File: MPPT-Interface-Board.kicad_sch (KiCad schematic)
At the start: 29 parts, among them J1 MPPT A, J2 MPPT X, J3 CarCAN In, J4 CarCAN Out, J5 FUSEBOX, Q1 PMV35EPER, U1 RI3-1209S

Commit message: uhm so why am i so stupid
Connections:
- net +12V: no longer C4.1
- net +12V_PROT: now also C4.1
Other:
- moved on the sheet: C3, C4
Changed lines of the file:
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@@
 	(wire
 		(pts
-			(xy 204.47 100.33) (xy 207.01 100.33)
+			(xy 204.47 100.33) (xy 208.28 100.33)
 		)
 		(stroke
@@
 	(wire
 		(pts
-			(xy 207.01 88.9) (xy 204.47 88.9)
+			(xy 208.28 88.9) (xy 204.47 88.9)
 		)
 		(stroke
@@
 	(wire
 		(pts
-			(xy 214.63 100.33) (xy 217.17 100.33)
+			(xy 215.9 100.33) (xy 219.71 100.33)
 		)
 		(stroke
@@
 	(wire
 		(pts
-			(xy 214.63 88.9) (xy 217.17 88.9)
+			(xy 215.9 88.9) (xy 219.71 88.9)
 		)
 		(stroke
@@
 	(wire
 		(pts
-			(xy 217.17 88.9) (xy 217.17 86.36)
+			(xy 219.71 88.9) (xy 219.71 86.36)
 		)
 		(stroke
@@
 	(wire
 		(pts
-			(xy 217.17 100.33) (xy 217.17 102.87)
+			(xy 219.71 100.33) (xy 219.71 102.87)
 		)
 		(stroke
@@
 	(rectangle
 		(start 198.12 78.74)
-		(end 223.52 114.3)
+		(end 226.06 114.3)
 		(stroke
 			(width 0)
@@
 		(exclude_from_sim no)
 		(at 198.12 110.49 0)
-		(size 25.4 3.81)
+		(size 27.94 3.81)
 		(stroke
 			(width 0)
@@
 	)
 	(symbol
+		(lib_id "power:+12V")
+		(at 204.47 86.36 0)
+		(unit 1)
+		(exclude_from_sim no)
+		(in_bom yes)
+		(on_board yes)
+		(dnp no)
+		(property "Reference" "#PWR021"
+			(at 204.47 90.17 0)
+			(effects
+				(font
+					(size 1.27 1.27)
+				)
+				(hide yes)
+			)
+		)
+		(property "Value" "+12V_PROT"
+			(at 198.882 82.55 0)
+			(effects
+				(font
+					(size 1.27 1.27)
+				)
+				(justify left)
+			)
+		)
+		(property "Footprint" ""
+			(at 204.47 86.36 0)
+			(effects
+				(font
+					(size 1.27 1.27)
+				)
+				(hide yes)
+			)
+		)
+		(property "Datasheet" ""
+			(at 204.47 86.36 0)
+			(effects
+				(font
+					(size 1.27 1.27)
+				)
+				(hide yes)
+			)
+		)
+		(property "Description" "Power symbol creates a global label with name \"+12V\""
+			(at 204.47 86.36 0)
+			(effects
+				(font
+					(size 1.27 1.27)
+				)
+				(hide yes)
+			)
+		)
+		(pin "1"
+		)
+		(instances
+			(project "MPPT-Interface-Board"
+				(path "/b7de5949-1fc3-44b6-95a7-0faccc8a2b33"
+					(reference "#PWR021")
+					(unit 1)
+				)
+			)
+		)
+	)
+	(symbol
 		(lib_id "power:GND")
 		(at 63.5 97.79 0)
@@
 	)
 	(symbol
-		(lib_id "power:+12V")
-		(at 204.47 86.36 0)
-		(unit 1)
-		(exclude_from_sim no)
-		(in_bom yes)
-		(on_board yes)
-		(dnp no)
-		(property "Reference" "#PWR021"
-			(at 204.47 90.17 0)
-			(effects
-				(font
-					(size 1.27 1.27)
-				)
-				(hide yes)
-			)
-		)
-		(property "Value" "+12V"
-			(at 201.676 82.55 0)
-			(effects
-				(font
-					(size 1.27 1.27)
-				)
-				(justify left)
-			)
-		)
-		(property "Footprint" ""
-			(at 204.47 86.36 0)
-			(effects
-				(font
-					(size 1.27 1.27)
-				)
-				(hide yes)
-			)
-		)
-		(property "Datasheet" ""
-			(at 204.47 86.36 0)
-			(effects
-				(font
-					(size 1.27 1.27)
-				)
-				(hide yes)
-			)
-		)
-		(property "Description" "Power symbol creates a global label with name \"+12V\""
-			(at 204.47 86.36 0)
-			(effects
-				(font
-					(size 1.27 1.27)
-				)
-				(hide yes)
-			)
-		)
-		(pin "1"
-		)
-		(instances
-			(project "MPPT-Interface-Board"
-				(path "/b7de5949-1fc3-44b6-95a7-0faccc8a2b33"
-					(reference "#PWR021")
-					(unit 1)
-				)
-			)
-		)
-	)
-	(symbol
 		(lib_id "Device:R")
 		(at 139.7 92.71 0)
@@
 	(symbol
 		(lib_id "power:GND")
-		(at 217.17 102.87 0)
+		(at 219.71 102.87 0)
 		(unit 1)
 		(exclude_from_sim no)
@@
 		(dnp no)
 		(property "Reference" "#PWR020"
-			(at 217.17 109.22 0)
+			(at 219.71 109.22 0)
 			(effects
 				(font
@@
 		)
 		(property "Value" "CGND"
-			(at 217.17 106.934 0)
+			(at 219.71 106.934 0)
 			(effects
 				(font
@@
 		)
 		(property "Footprint" ""
-			(at 217.17 102.87 0)
+			(at 219.71 102.87 0)
 			(effects
 				(font
@@
 		)
 		(property "Datasheet" ""
-			(at 217.17 102.87 0)
+			(at 219.71 102.87 0)
 			(effects
 				(font
@@
 		)
 		(property "Description" "Power symbol creates a global label with name \"GND\" , ground"
-			(at 217.17 102.87 0)
+			(at 219.71 102.87 0)
 			(effects
 				(font
@@
 	(symbol
 		(lib_id "Device:C")
-		(at 210.82 88.9 90)
+		(at 212.09 88.9 90)
 		(unit 1)
 		(exclude_from_sim no)
@@
 		(dnp no)
 		(property "Reference" "C4"
-			(at 210.82 82.804 90)
+			(at 212.09 82.804 90)
 			(effects
 				(font
@@
 		)
 		(property "Value" "470p"
-			(at 210.82 85.09 90)
+			(at 212.09 85.09 90)
 			(effects
 				(font
@@
 		)
 		(property "Footprint" "Capacitor_SMD:C_0805_2012Metric"
-			(at 214.63 87.9348 0)
+			(at 215.9 87.9348 0)
 			(effects
 				(font
@@
 		)
 		(property "Datasheet" "~"
-			(at 210.82 88.9 0)
+			(at 212.09 88.9 0)
 			(effects
 				(font
@@
 		)
 		(property "Description" "Unpolarized capacitor"
-			(at 210.82 88.9 0)
+			(at 212.09 88.9 0)
 			(effects
 				(font
@@
 		)
 		(property "P/N" "08053C471JAT2A"
-			(at 210.82 88.9 0)
+			(at 212.09 88.9 0)
 			(effects
 				(font
@@
 	(symbol
 		(lib_id "power:+12V")
-		(at 217.17 86.36 0)
+		(at 219.71 86.36 0)
 		(unit 1)
 		(exclude_from_sim no)
@@
 		(dnp no)
 		(property "Reference" "#PWR022"
-			(at 217.17 90.17 0)
+			(at 219.71 90.17 0)
 			(effects
 				(font
@@
 		)
 		(property "Value" "V_CAN"
-			(at 214.122 82.55 0)
+			(at 216.662 82.55 0)
 			(effects
 				(font
@@
 		)
 		(property "Footprint" ""
-			(at 217.17 86.36 0)
+			(at 219.71 86.36 0)
 			(effects
 				(font
@@
 		)
 		(property "Datasheet" ""
-			(at 217.17 86.36 0)
+			(at 219.71 86.36 0)
 			(effects
 				(font
@@
 		)
 		(property "Description" "Power symbol creates a global label with name \"+12V\""
-			(at 217.17 86.36 0)
+			(at 219.71 86.36 0)
 			(effects
 				(font
@@
 	(symbol
 		(lib_id "Device:C")
-		(at 210.82 100.33 90)
+		(at 212.09 100.33 90)
 		(unit 1)
 		(exclude_from_sim no)
@@
 		(dnp no)
 		(property "Reference" "C3"
-			(at 210.82 94.234 90)
+			(at 212.09 94.234 90)
 			(effects
 				(font
@@
 		)
 		(property "Value" "330p"
-			(at 210.82 96.266 90)
+			(at 212.09 96.266 90)
 			(effects
 				(font
@@
 		)
 		(property "Footprint" "Capacitor_SMD:C_0805_2012Metric"
-			(at 214.63 99.3648 0)
+			(at 215.9 99.3648 0)
 			(effects
 				(font
@@
 		)
 		(property "Datasheet" "~"
-			(at 210.82 100.33 0)
+			(at 212.09 100.33 0)
 			(effects
 				(font
@@
 		)
 		(property "Description" "Unpolarized capacitor"
-			(at 210.82 100.33 0)
+			(at 212.09 100.33 0)
 			(effects
 				(font
@@
 		)
 		(property "P/N" "08053A331JAT2A"
-			(at 210.82 100.33 0)
+			(at 212.09 100.33 0)
 			(effects
 				(font

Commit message: initial layout (unrouted)
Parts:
- added H1, H2, H3, H4: MountingHole, MountingHole:MountingHole_3mm, symbol Mechanical:MountingHole
- TP6: value CGND -> CGND2
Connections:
- net CAN_H: no longer R1.2
- net CAN_H2: now also R1.2
- net CAN_L: no longer JP1.2 (B)
- net CAN_L2: now also JP1.2 (B)
- net CGND: no longer TP6.1
- net CGND2: now also TP6.1

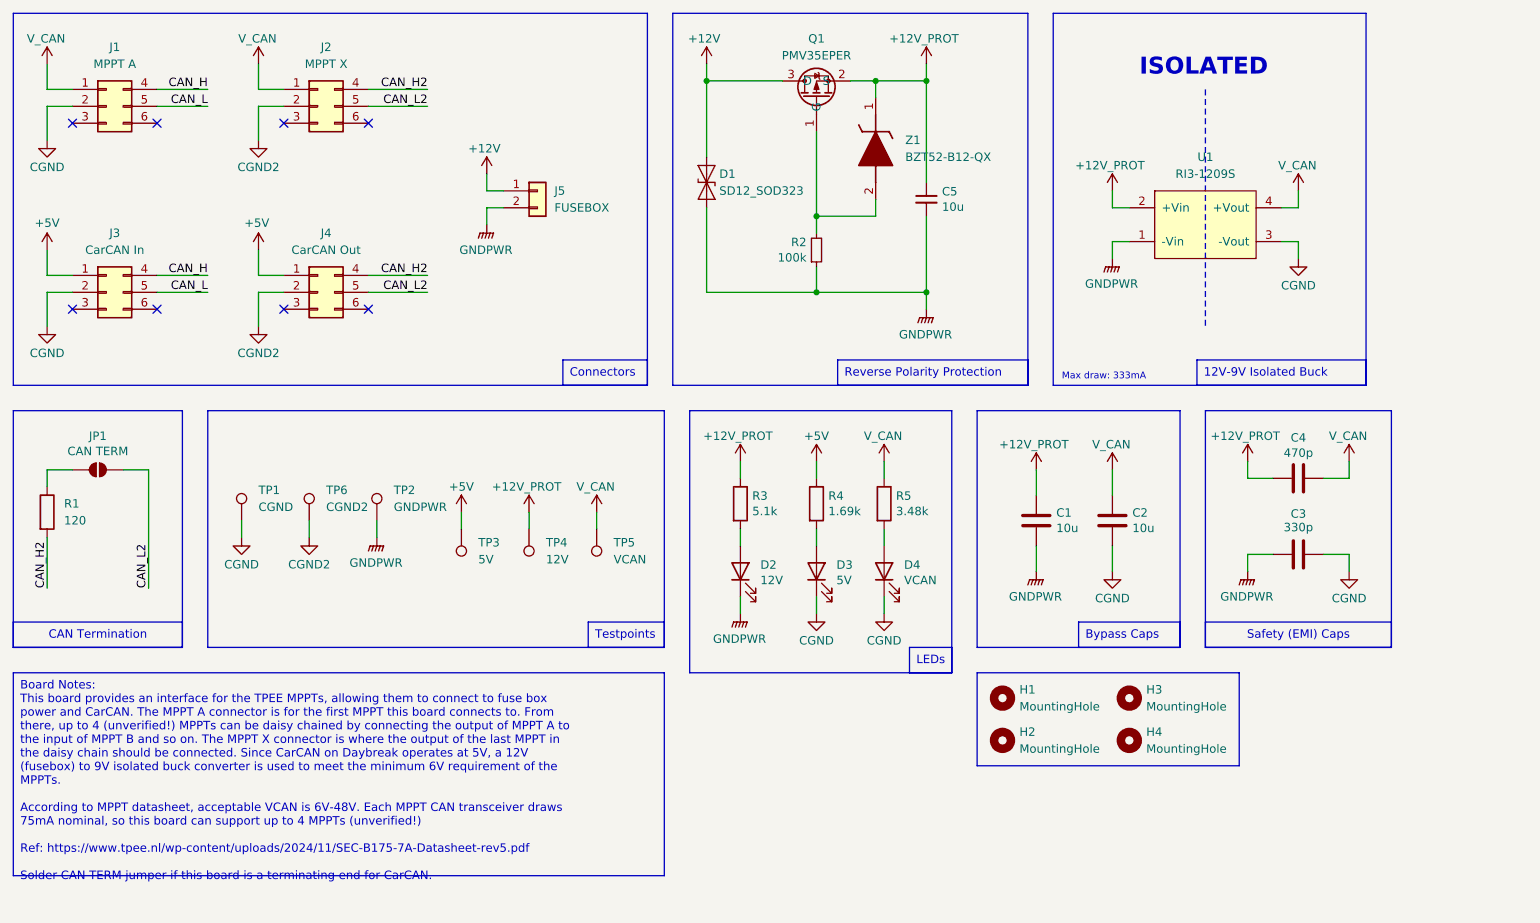
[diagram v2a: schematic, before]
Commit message: change carcan to 4 pin & add start termination
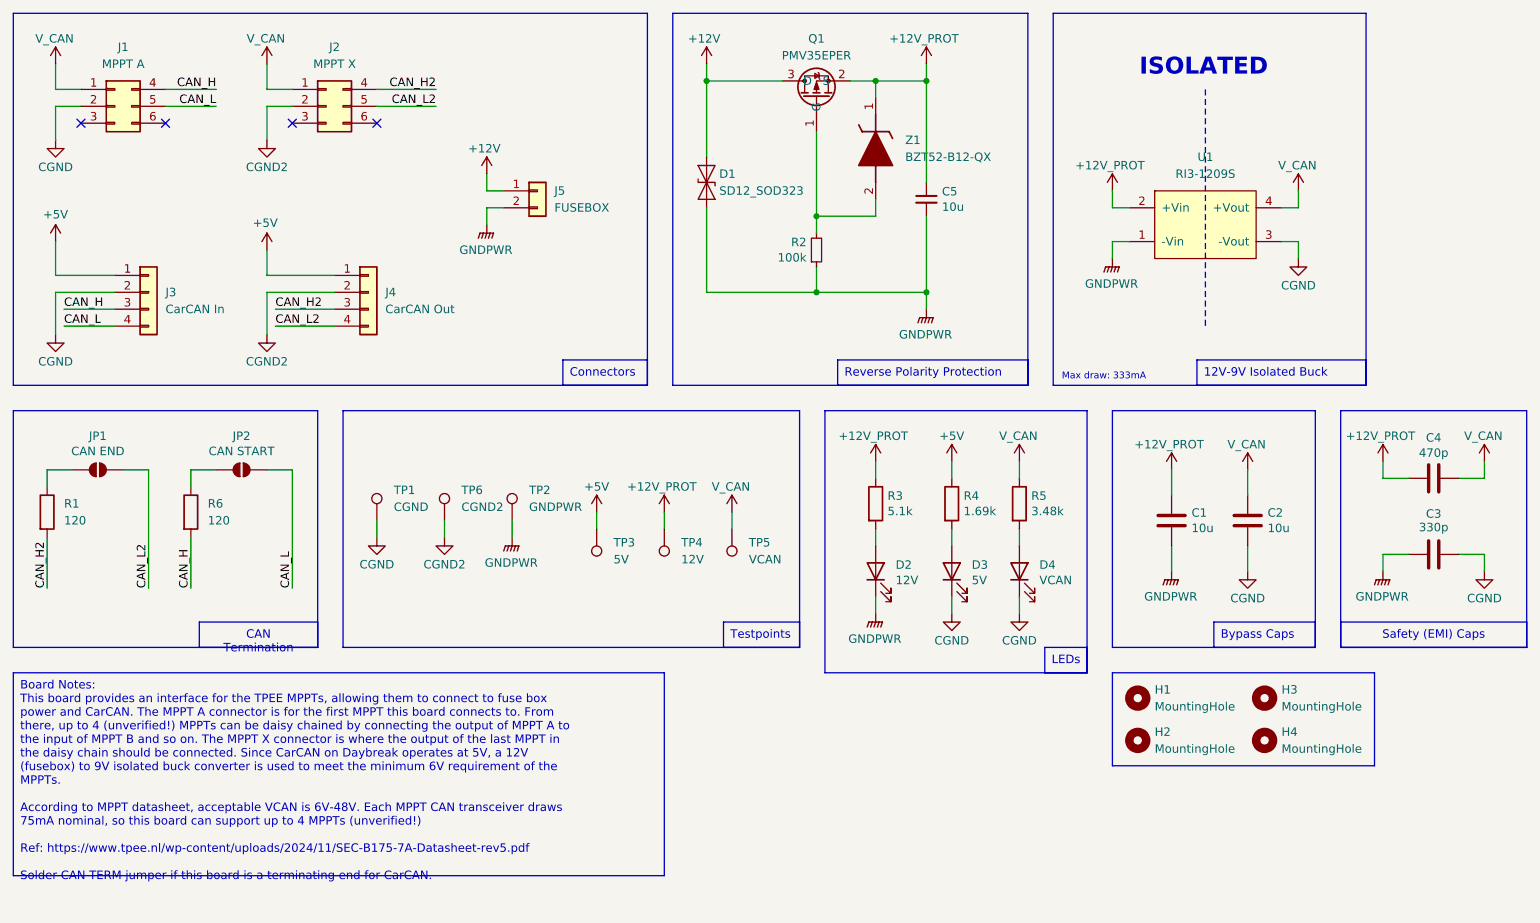
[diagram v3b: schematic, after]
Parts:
- added JP2: CAN START, Jumper:SolderJumper-2_P1.3mm_Open_TrianglePad1.0x1.5mm, symbol Jumper:SolderJumper_2_Open
- added R6: 120, Resistor_SMD:R_0805_2012Metric, symbol Device:R
- J3, J4: footprint Connector_Molex:Molex_Micro-Fit_3.0_43045-0612_2x03_P3.00mm_Vertical -> UTSVT_Connectors:Molex_MicroFit3.0_1x4xP3.00mm_PolarizingPeg_Vertical; symbol Connector_Generic:Conn_02x03_Top_Bottom -> Connector_Generic:Conn_01x04; P/N 430450612 -> 0436500415
- JP1: value CAN TERM -> CAN END
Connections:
- net CAN_H: now also J3.3 (Pin_3), R6.2; no longer J3.4 (Pin_4)
- net CAN_H2: now also J4.3 (Pin_3); no longer J4.4 (Pin_4)
- net CAN_L: now also J3.4 (Pin_4), JP2.2 (B); no longer J3.5 (Pin_5)
- net CAN_L2: now also J4.4 (Pin_4); no longer J4.5 (Pin_5)
- new net: JP2.1 (A), R6.1
- no-connect marks 8 -> 4
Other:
- moved on the sheet: C1, C2, C3, C4, D2, D3, D4, H1, H2, H3, H4, J1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

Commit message: redo layout/routing/silks
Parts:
- J3, J4: footprint UTSVT_Connectors:Molex_MicroFit3.0_1x4xP3.00mm_PolarizingPeg_Vertical -> UTSVT-Connectors:Molex_MicroFit3.0_1x4xP3.00mm_PolarizingPeg_Vertical
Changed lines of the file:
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@@
 			)
 		)
-		(property "Footprint" "UTSVT_Connectors:Molex_MicroFit3.0_1x4xP3.00mm_PolarizingPeg_Vertical"
+		(property "Footprint" "UTSVT-Connectors:Molex_MicroFit3.0_1x4xP3.00mm_PolarizingPeg_Vertical"
 			(at 72.39 60.96 0)
 			(effects
@@
 			)
 		)
-		(property "Footprint" "UTSVT_Connectors:Molex_MicroFit3.0_1x4xP3.00mm_PolarizingPeg_Vertical"
+		(property "Footprint" "UTSVT-Connectors:Molex_MicroFit3.0_1x4xP3.00mm_PolarizingPeg_Vertical"
 			(at 39.37 60.96 0)
 			(effects

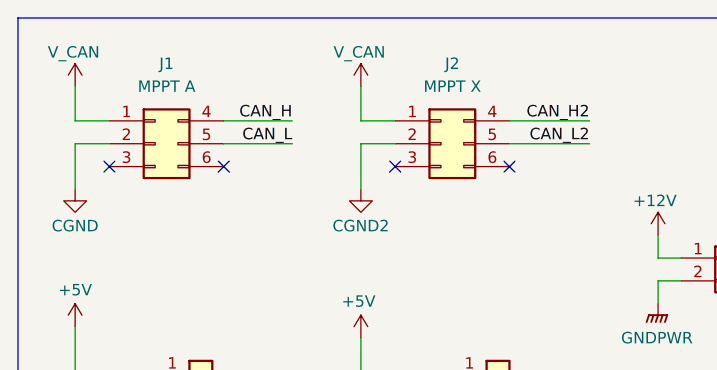
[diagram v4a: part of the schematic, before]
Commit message: lakshay make board black pls
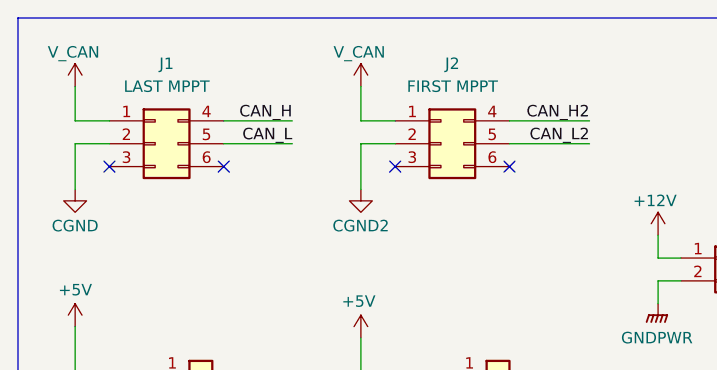
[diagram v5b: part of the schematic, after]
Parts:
- J1: value MPPT A -> LAST MPPT
- J2: value MPPT X -> FIRST MPPT
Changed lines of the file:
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@@
 			)
 		)
-		(property "Value" "MPPT A"
+		(property "Value" "LAST MPPT"
 			(at 35.56 26.67 0)
 			(effects
@@
 			)
 		)
-		(property "Value" "MPPT X"
+		(property "Value" "FIRST MPPT"
 			(at 67.31 26.67 0)
 			(effects

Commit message: wow
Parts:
- J1: value LAST MPPT -> FIRST MPPT
- J2: value FIRST MPPT -> LAST MPPT
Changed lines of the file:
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@@
 			)
 		)
-		(property "Value" "LAST MPPT"
+		(property "Value" "FIRST MPPT"
 			(at 35.56 26.67 0)
 			(effects
@@
 			)
 		)
-		(property "Value" "FIRST MPPT"
+		(property "Value" "LAST MPPT"
 			(at 67.31 26.67 0)
 			(effects
